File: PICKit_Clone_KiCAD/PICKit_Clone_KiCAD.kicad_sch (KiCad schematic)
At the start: 40 parts, among them J1 USB_C_Receptacle_USB2.0_16P, J2 Conn_02x03_Counter_Clockwise, Q1 MMBT3904, Q2 Si2319CDS, U1 PIC18F14K50-ESS, U2 MC34063AD, U3 LM1117MP-5.0, Y1 16MHz

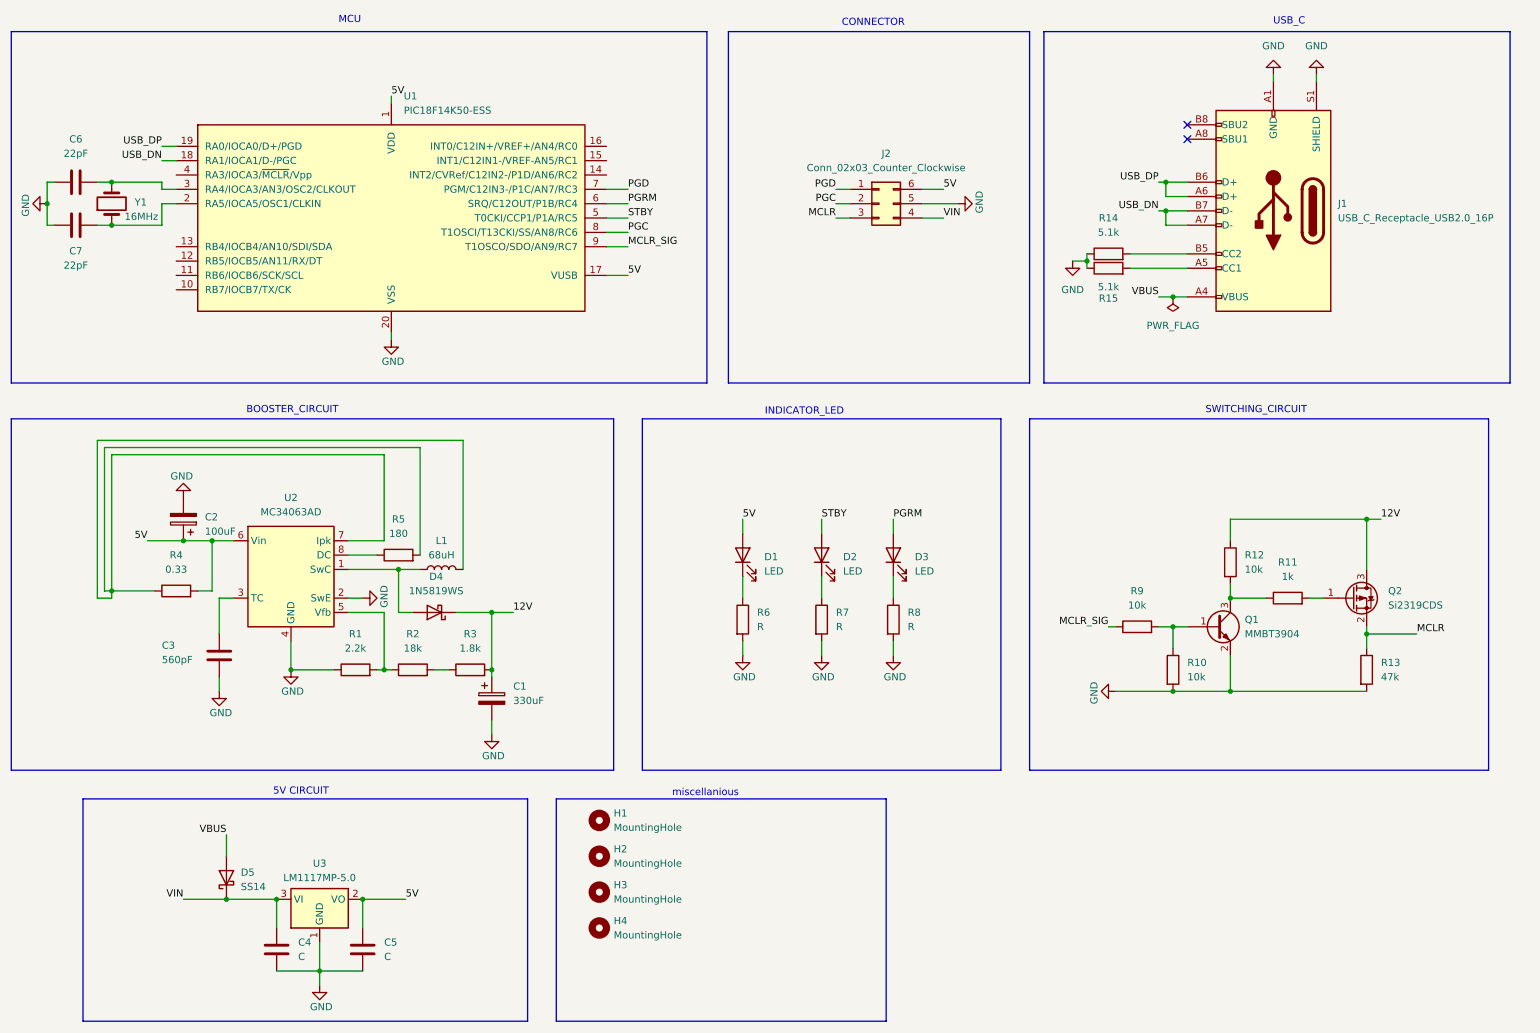
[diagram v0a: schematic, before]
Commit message: PCB and Design update
1) PCB has been modified to include pads for initial programming of the MCU
2)cover has been modified according to the new size of the PCB
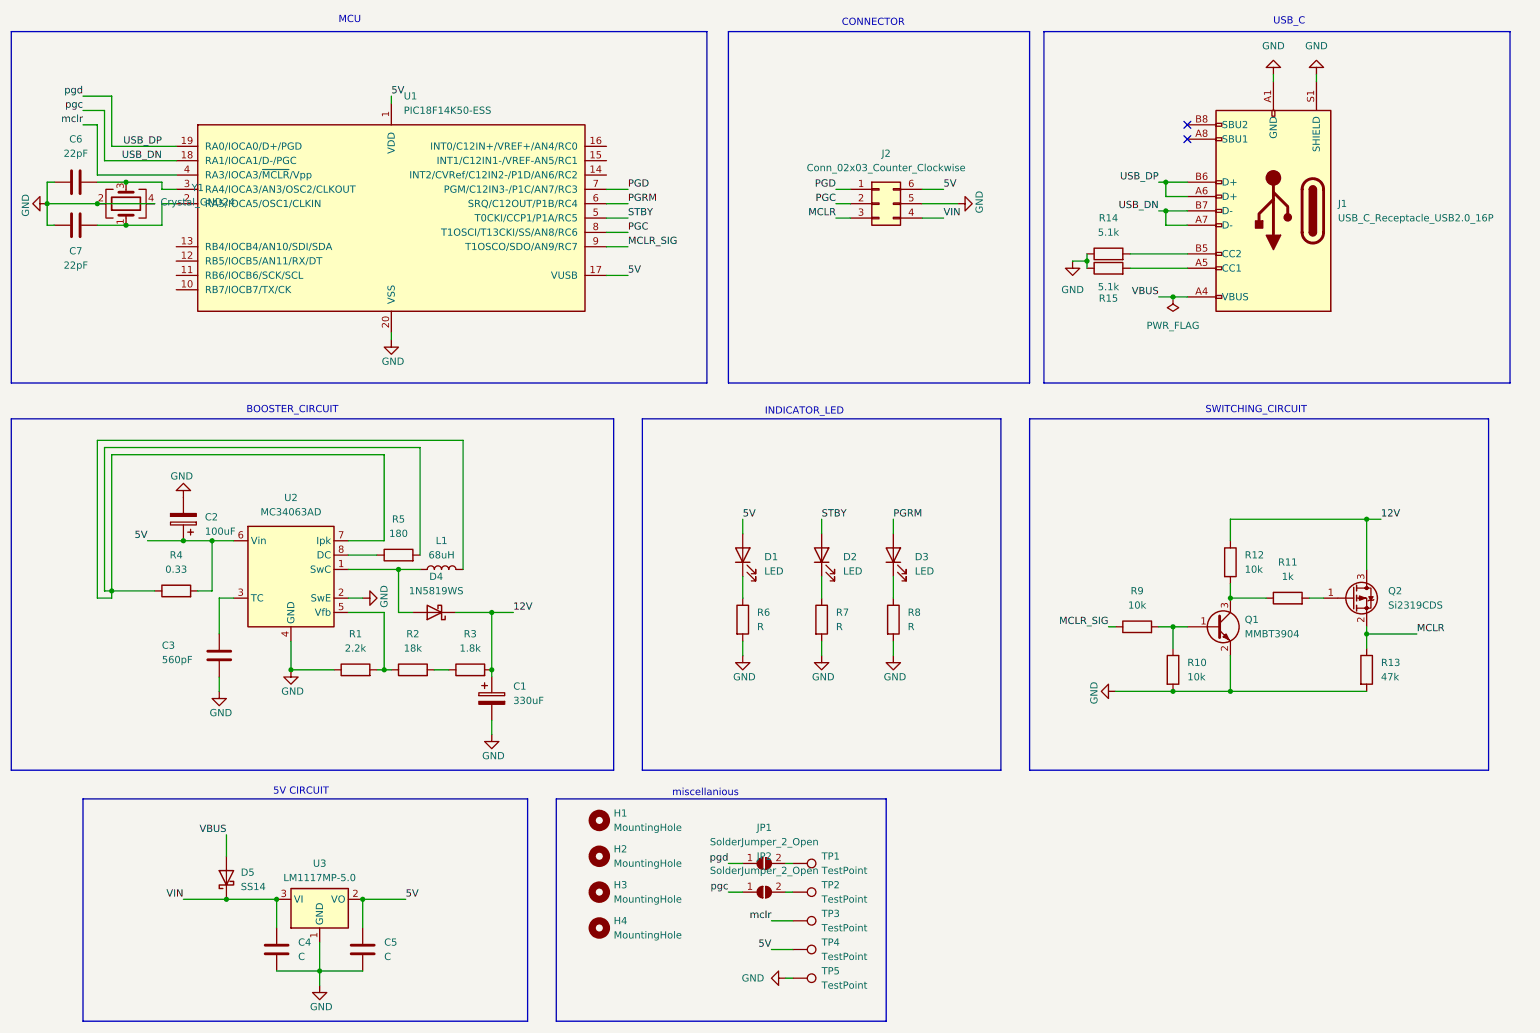
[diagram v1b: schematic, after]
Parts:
- removed Y1: 16MHz, Crystal:Crystal_SMD_HC49-SD, symbol Device:Crystal
- added JP1, JP2: SolderJumper_2_Open, Jumper:SolderJumper-2_P1.3mm_Open_Pad1.0x1.5mm, symbol Jumper:SolderJumper_2_Open
- added TP1, TP2, TP3, TP4, TP5: TestPoint, TestPoint:TestPoint_Pad_D1.0mm, symbol Connector:TestPoint
- added Y1: Crystal_GND24, Crystal:Crystal_SMD_3225-4Pin_3.2x2.5mm_HandSoldering, symbol Device:Crystal_GND24
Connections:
- net 5V: now also TP4.1
- net GND: now also TP5.1, Y1.2, Y1.4
- net USB_DN: now also JP2.1 (A)
- net USB_DP: now also JP1.1 (A)
- net at C7.2, U1.2 (RA5/IOCA5/OSC1/CLKIN): now also Y1.1
- net at C6.2, U1.3 (RA4/IOCA3/AN3/OSC2/CLKOUT): now also Y1.3
- net mclr: now reaches U1.4 (RA3/IOCA3/~{MCLR}/Vpp)
- net mclr: now also TP3.1
- new net: JP2.2 (B), TP2.1
- new net: JP1.2 (B), TP1.1
